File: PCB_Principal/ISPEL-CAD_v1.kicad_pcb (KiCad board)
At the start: 2 copper layers, 130 x 160 mm, 173 parts, among them J1 Vin, J10 E1, J11 S1, J12 E2, J13 S2, J14 FRENTE, J15 PRUEBA_5V, J16 V5, J17 VREG, J2 GND_NUCLEO, J3 CN8_NUCLEO, J4 CN9_NUCLEO, J5 GND_NUCLEO, J6 GND_NUCLEO, J7 CN7_NUCLEO, J8 CN10_NUCLEO, J9 GND_NUCLEO, Q201 BC807, Q202 BC559C, Q203 BC549C, Q204 BC549C, Q205 BC559C, Q206 2SD882, Q207 2SB772, Q251 BC807, Q252 BC559C, Q253 BC549C, Q254 BC549C, Q255 BC559C, Q256 2SD882, Q257 2SB772, U1 LM350_TO220, U101 TL071, U151 TL071, U2 LM350_TO220, U201 LM318, U251 LM318, U3 LM337_TO220, U301 TLV3501AID, U4 LM1117DT-5.0, U5 TL431DBZ

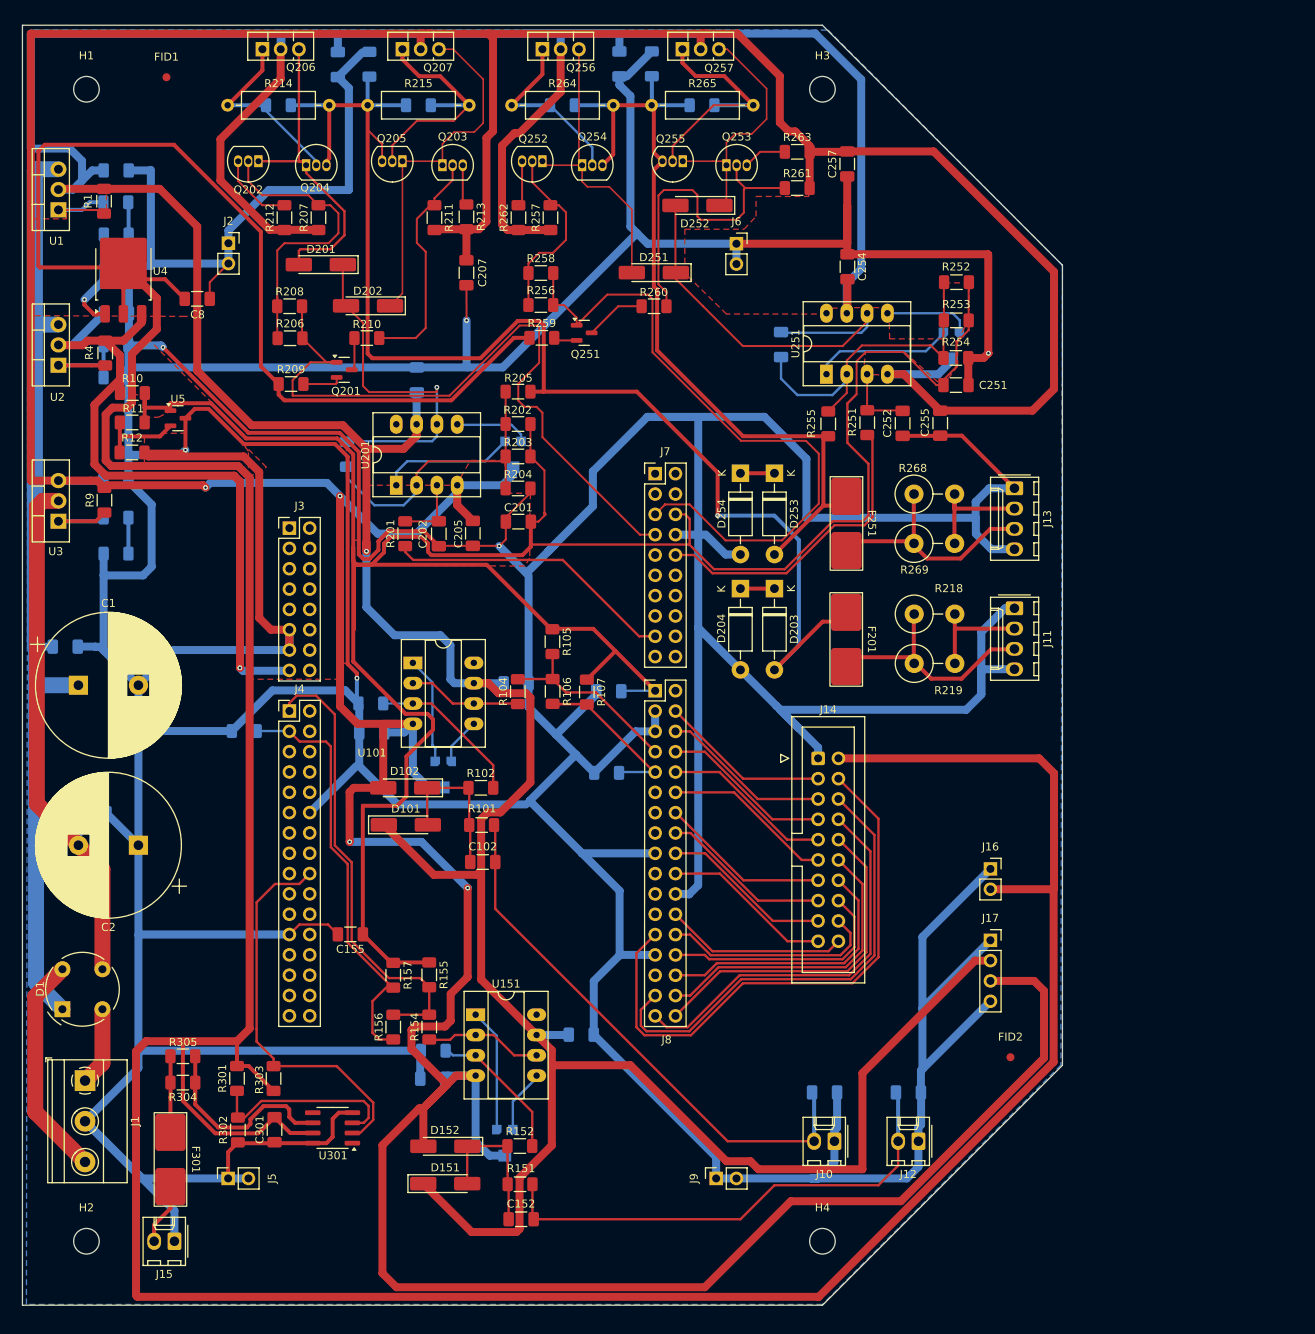
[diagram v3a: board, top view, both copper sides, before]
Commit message: Rellenos de blindaje.
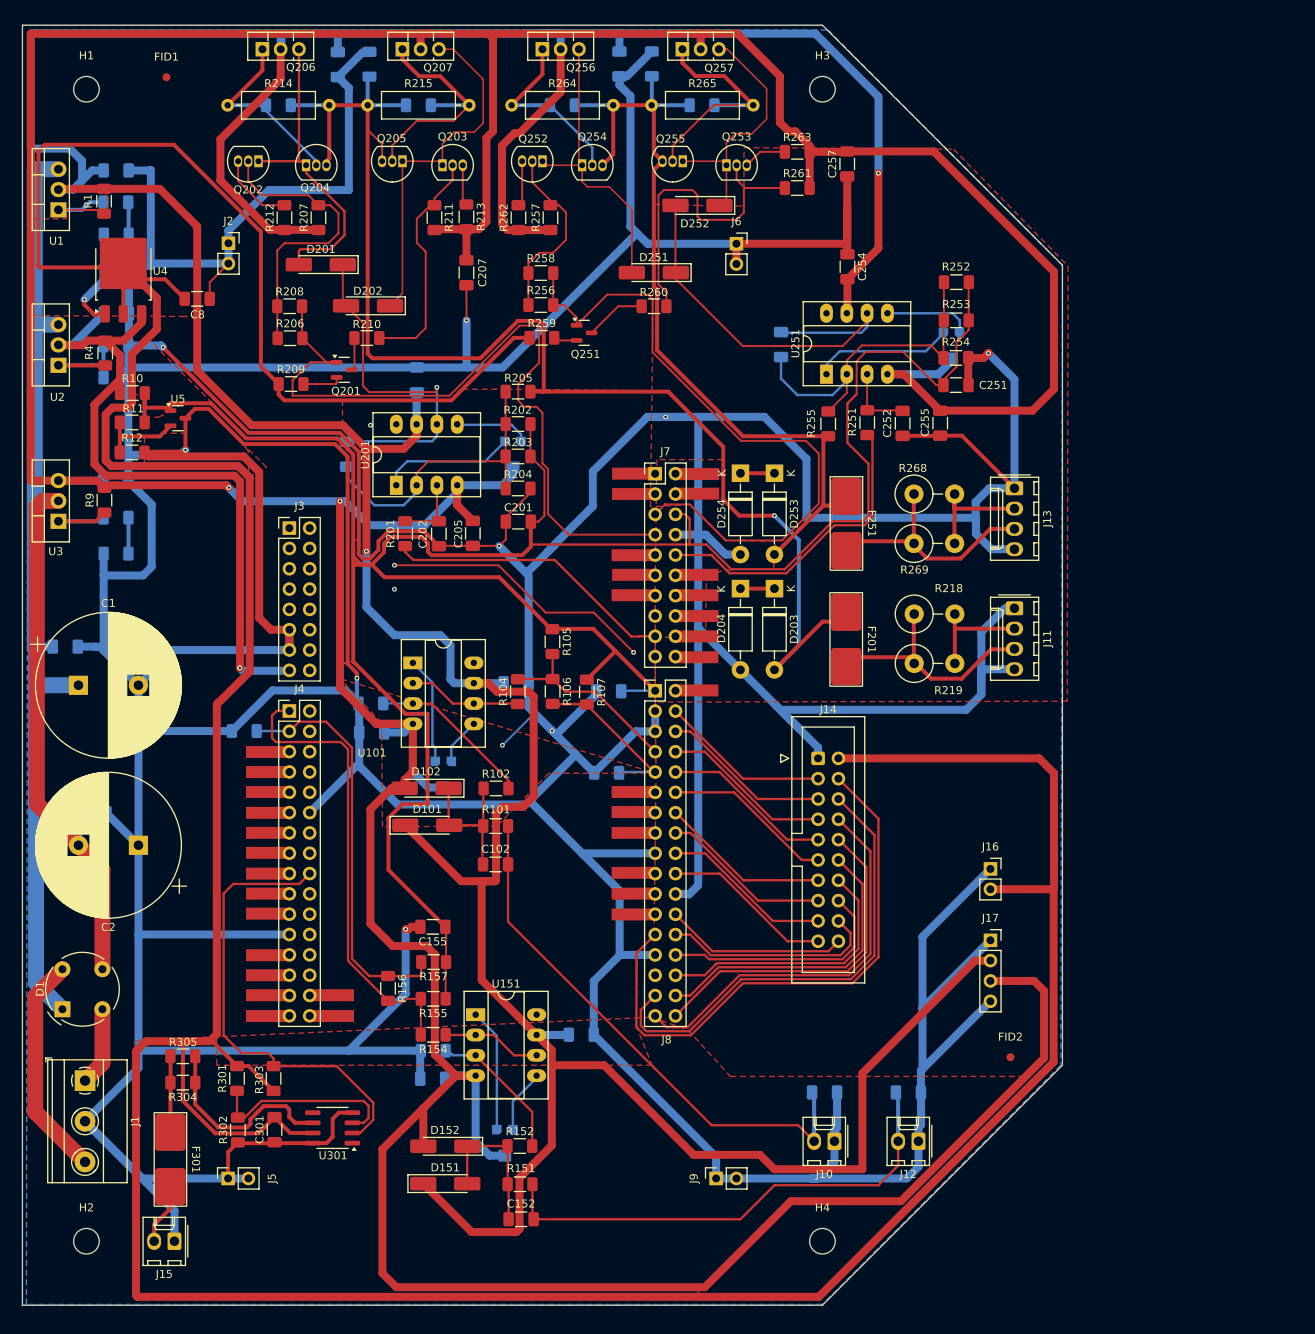
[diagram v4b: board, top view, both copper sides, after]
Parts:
- moved C155 10.4 mm to (81.3, 142.7)
- moved R157 5.31 mm to (81.4, 147.1), turned to 180 degrees
- moved R156 4.87 mm to (75.7, 150.4), turned to 90 degrees
- moved R155 3.04 mm to (81.3, 151.7), turned to 180 degrees
- moved D102 2.68 mm to (80.5, 125.4)
- moved D101 2.68 mm to (80.6, 130.0)
- moved R102 1.90 mm to (89.2, 125.4)
- moved R101 1.75 mm to (89.2, 130.1)
- moved C102 1.63 mm to (89.1, 134.9)
- moved R154 1.09 mm to (81.3, 156.2), turned to 180 degrees
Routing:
- net GND: track 1315.9 -> 1357.4 mm, vias 7 -> 15
- net VEE: track 659.4 -> 641.4 mm, vias 4 -> 2
- net V33REF: track 324.4 -> 314.4 mm
- net PRUEBA: track 49.3 -> 57.7 mm
- net CTRL_S1: track 88.6 -> 93.8 mm
- net VCC: track 574.4 -> 572.1 mm, vias 1 -> 2
- net ADC2_C20: track 53.7 -> 51.4 mm
- net /Entrada 2/VOA: track 14.7 -> 12.6 mm
- net Net-(D101-A): track 19.2 -> 17.9 mm
- net Net-(Q202-B): track 38.6 -> 37.5 mm
- net Net-(U101-+): track 19.8 -> 20.9 mm
- net E1: track 68.6 -> 67.8 mm
- net /Salida 1/SALIDA0: track 170.6 -> 171.3 mm

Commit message: Corrección de conector.
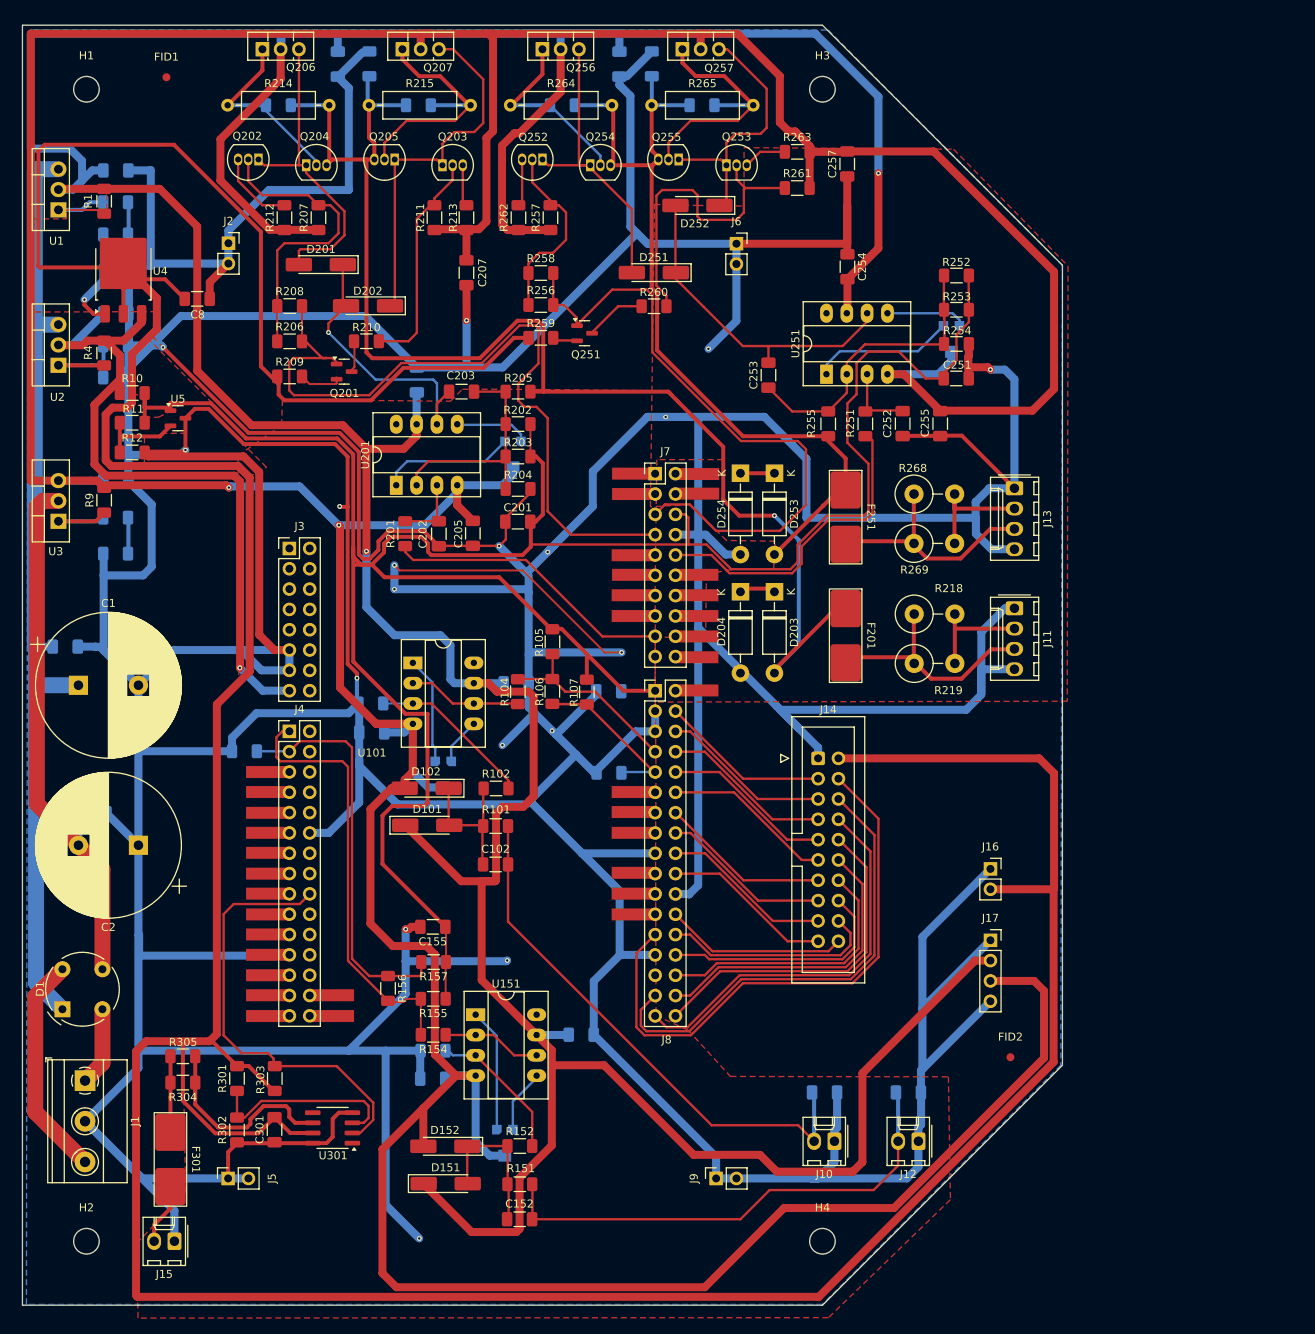
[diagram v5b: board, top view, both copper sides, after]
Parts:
- C203, C253: moved to F.Cu
- J4: footprint Libreria_ISPEL:PinSocket_2x16_P2.54mm_Vertical_impar-par -> Libreria_ISPEL:PinSocket_2x15_P2.54mm_Vertical_impar-par
- moved C203 16.3 mm to (84.9, 75.8), turned to 180 degrees
- moved C253 4.14 mm to (123.2, 73.7)
- moved J3 2.54 mm to (63.4, 95.4)
- moved J4 2.54 mm to (63.4, 118.3)
- moved R158 2.53 mm to (57.8, 120.8)
- moved R254 1.75 mm to (146.8, 69.8)
- moved R253 1.33 mm to (146.8, 65.6)
- moved Q254 1.01 mm to (101.0, 47.5)
- moved Q205 1.00 mm to (76.5, 46.8)
- moved R209 0.97 mm to (63.4, 73.9)
- moved C251 0.83 mm to (146.7, 74.2)
- moved R252 0.83 mm to (146.8, 61.3)
- moved RV251 0.83 mm to (146.1, 69.2)
- moved F251 0.79 mm to (132.9, 91.5)
- moved Q255 0.56 mm to (112.0, 46.8)
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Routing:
- net GND: track 1357.4 -> 1461.8 mm, vias 15 -> 19
- net /Salida 2/VOA: track 52.3 -> 41.0 mm
- net /Salida 1/VOA: track 44.2 -> 35.6 mm
- net Net-(U201--): track 38.6 -> 30.4 mm
- net /Salida 1/SALIDA0: track 171.3 -> 166.0 mm
- net Net-(U251--): track 44.3 -> 39.3 mm
- net ADC2_C10: track 57.6 -> 54.1 mm
- net CTRL_S2: track 83.5 -> 80.6 mm
- net VEE: track 641.4 -> 638.6 mm
- net PRUEBA: track 57.7 -> 55.1 mm
- net /Salida 2/VBN: track 31.9 -> 34.4 mm
- net Net-(Q205-B): track 30.5 -> 31.8 mm
- net ADC2_C20: track 51.4 -> 50.4 mm
- net CTRL_S1: track 93.8 -> 94.8 mm
- net V7: track 88.0 -> 89.1 mm
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
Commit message: Corrigiendo hojas de datos.
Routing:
- net CTRL_S1: track 94.8 -> 95.6 mm
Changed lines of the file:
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@@
 		(tags "capacitor handsolder")
 		(property "Reference" "C203"
-			(at 0.1 2 360)
+			(at 0.1 2 0)
 			(layer "F.SilkS")
 			(effects
@@
 		)
 		(property "Value" "10pF"
-			(at 0 1.85 360)
+			(at 0 1.85 0)
 			(layer "F.Fab")
 			(effects
@@
 		)
 		(fp_text user "${REFERENCE}"
-			(at 0 0 360)
+			(at 0 0 0)
 			(layer "F.Fab")
 			(effects
@@
 	)
 	(segment
+		(start 64.95 69.5125)
+		(end 66.05 70.6125)
+		(width 0.3)
+		(layer "F.Cu")
+		(net 75)
+	)
+	(segment
 		(start 92.122816 67.535)
 		(end 94.185 67.535)
@@
 	)
 	(segment
-		(start 68.05 71.6)
-		(end 67.475 71.6)
+		(start 92.76 77.7)
+		(end 94.25 77.7)
 		(width 0.3)
 		(layer "F.Cu")
@@
 	)
 	(segment
-		(start 92.76 77.7)
-		(end 94.25 77.7)
-		(width 0.3)
+		(start 64.95 69.5125)
+		(end 64.95 65.125)
+		(width 0.25)
 		(layer "F.Cu")
 		(net 75)
@@
 	)
 	(segment
-		(start 67.475 71.6)
-		(end 65 69.125)
+		(start 66.05 70.6125)
+		(end 66.05 71.6)
 		(width 0.3)
 		(layer "F.Cu")
@@
 	)
 	(segment
-		(start 64.95 65.125)
-		(end 64.95 69.075)
-		(width 0.25)
-		(layer "F.Cu")
-		(net 75)
-	)
-	(segment
 		(start 94.5 72.29)
 		(end 91.98 74.81)
@@
 	)
 	(segment
-		(start 68.05 71.6)
-		(end 68.75 71.6)
-		(width 0.25)
+		(start 66.05 71.6)
+		(end 68.05 71.6)
+		(width 0.3)
 		(layer "F.Cu")
 		(net 75)
 	)
 	(segment
-		(start 64.95 69.075)
-		(end 65 69.125)
+		(start 68.05 71.6)
+		(end 68.75 71.6)
 		(width 0.25)
 		(layer "F.Cu")
@@
 			(thermal_gap 0.5)
 			(thermal_bridge_width 0.5)
-			(smoothing fillet)
-			(radius 1)
 		)
 		(polygon

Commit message: Actualización de hojas de datos.
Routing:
- net GND: track 1461.8 -> 1466.8 mm, vias 19 -> 20
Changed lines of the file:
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@@
+	)
+	(via
+		(at 88.45 77.7)
+		(size 0.6)
+		(drill 0.3)
+		(layers "F.Cu" "B.Cu")
+		(free yes)
+		(net 2)
 	)
 	(via
@@
 	)
 	(segment
+		(start 88.25 72.775)
+		(end 88.25 77.5)
+		(width 1)
+		(layer "B.Cu")
+		(net 2)
+	)
+	(segment
 		(start 44.625 120.75)
 		(end 44.625 118.225)
@@
 	)
 	(segment
+		(start 88.25 72.775)
+		(end 90.035 72.775)
+		(width 1)
+		(layer "B.Cu")
+		(net 2)
+	)
+	(segment
 		(start 95.65 95.84)
 		(end 95.65 95.85)
@@
 	)
 	(segment
+		(start 88.25 77.5)
+		(end 88.45 77.7)
+		(width 1)
+		(layer "B.Cu")
+		(net 2)
+	)
+	(segment
 		(start 72.1 121.85)
 		(end 72.1 127.15)
@@
 	)
 	(segment
+		(start 85.63 72.775)
+		(end 88.25 72.775)
+		(width 1)
+		(layer "B.Cu")
+		(net 2)
+	)
+	(segment
 		(start 116.71 171.4775)
 		(end 101.4125 156.18)
@@
 		(width 1)
 		(layer "B.Cu")
-		(net 2)
-	)
-	(segment
-		(start 85.63 72.775)
-		(end 90.035 72.775)
-		(width 1)
-		(layer "B.Cu")
